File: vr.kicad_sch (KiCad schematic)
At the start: 23 parts, among them U2 ST1PS02CQTR, U3 ST1PS02CQTR, U301 LDLN025M12R, U304 LM2664M6_NOPB

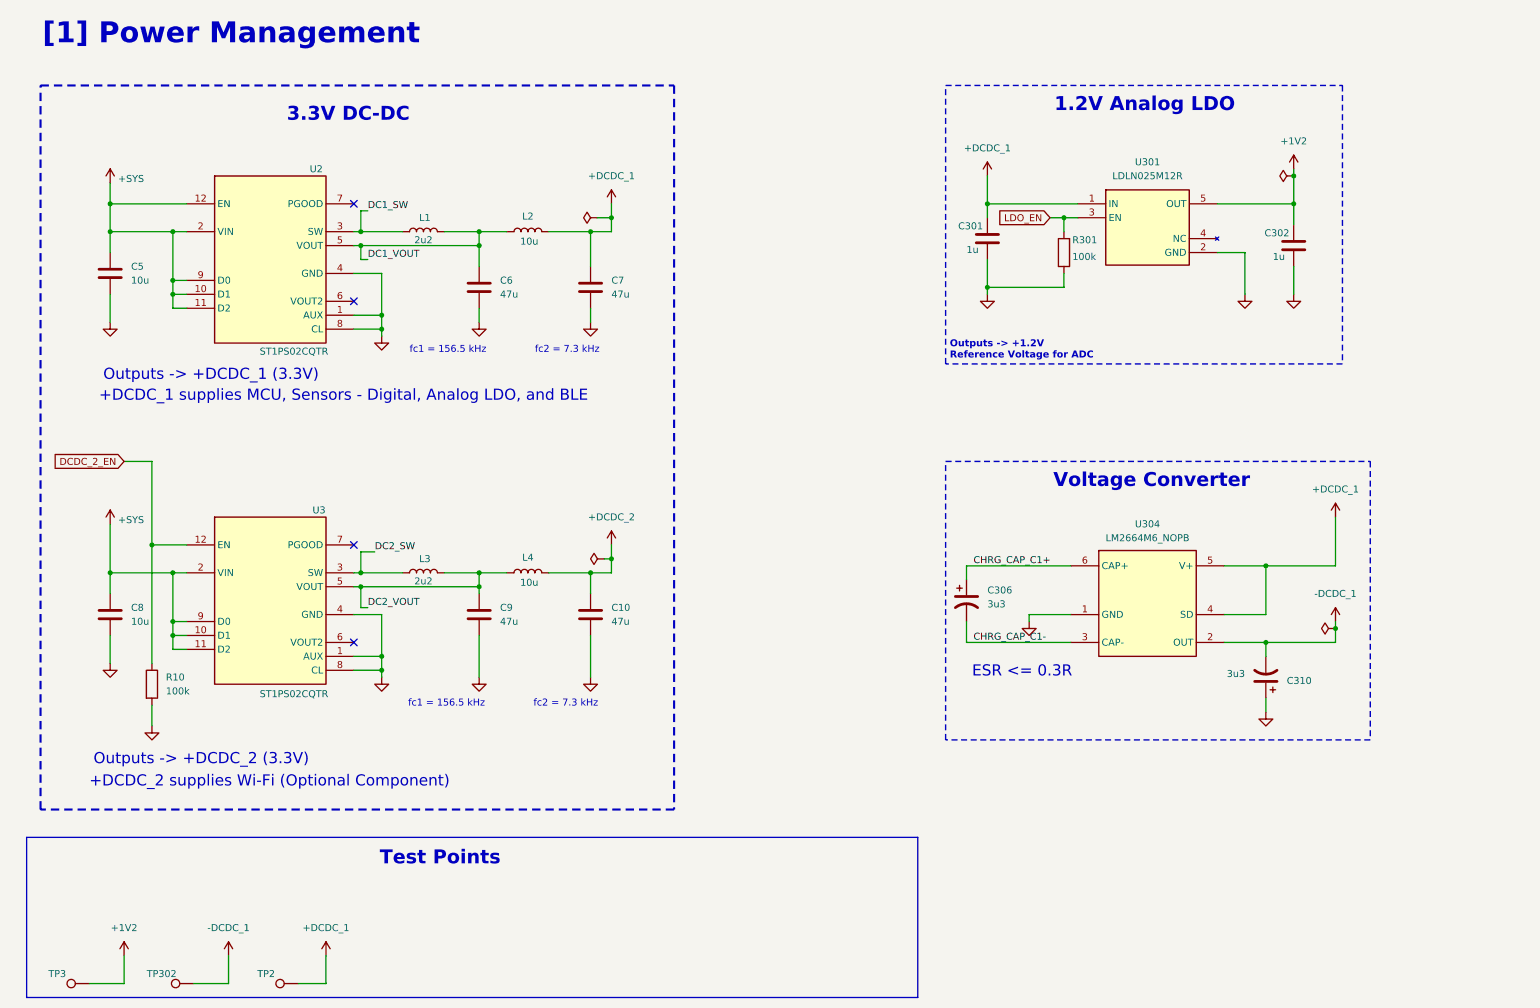
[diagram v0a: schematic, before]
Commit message: only usb powered
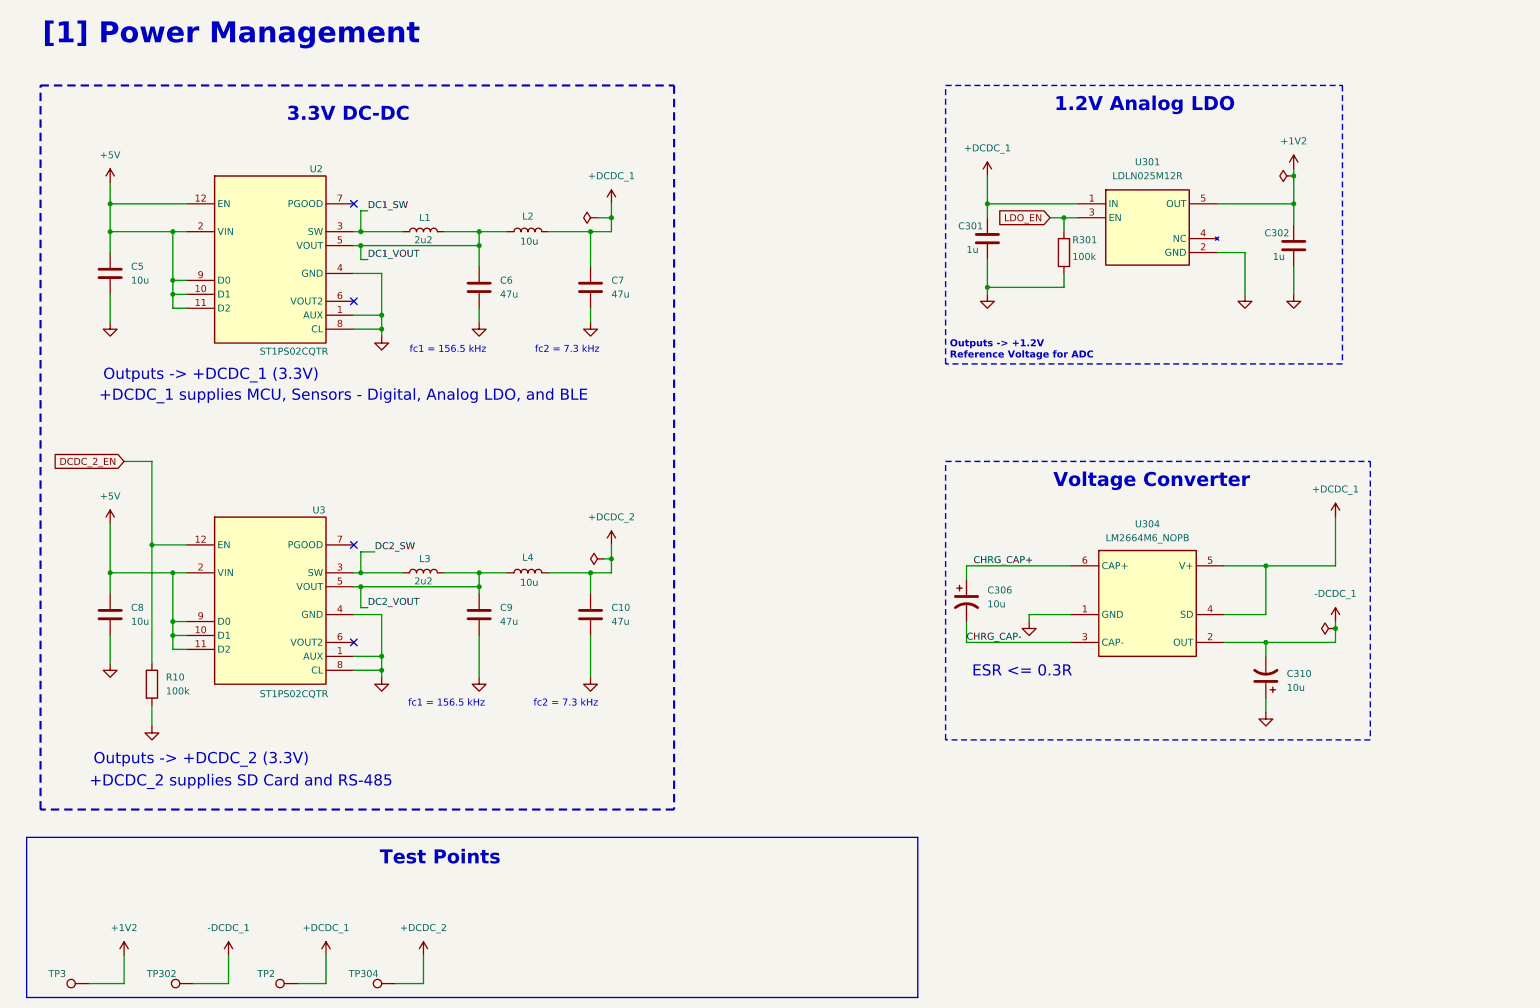
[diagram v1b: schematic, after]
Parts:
- added TP304: TestPoint, TestPoint:TestPoint_Loop_D3.50mm_Drill1.4mm_Beaded, symbol Connector:TestPoint
- C306, C310: value 3u3 -> 10u; footprint Capacitor_SMD:CP_Elec_4x3.9 -> EMS:10SVPS10M; Manufacturer_Name Nichicon -> Panasonic; Manufacturer_Part_Number UZG1H3R3MCL1GB -> 10SVPS10M
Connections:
- net +DCDC_2: now also TP304.1
- net +SYS renamed +5V
- net CHRG_CAP_C1+ renamed CHRG_CAP+
- net CHRG_CAP_C1- renamed CHRG_CAP-
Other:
- note added: "+DCDC_2 supplies SD Card and RS-485"
- note removed: "+DCDC_2 supplies Wi-Fi (Optional Component)"

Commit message: components with distributor links added
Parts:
- C10, C6, C7, C9: Distributor_Link (none) -> https://www.mouser.com/ProductDetail/KYOCERA-AVX/KGM15CR50J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; Manufacturer_Name (none) -> KYOCERA AVX; Manufacturer_Part_Number (none) -> KGM15CR50J476MT
- C301, C302: footprint Capacitor_SMD:C_0603_1608Metric -> Capacitor_SMD:C_0402_1005Metric; Distributor_Link (none) -> https://www.mouser.com/ProductDetail/KYOCERA-AVX/KGM05AR70J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; Manufacturer_Name (none) -> KYOCERA AVX; Manufacturer_Part_Number (none) -> KGM05AR70J105KH
- C306, C310: Distributor_Link (none) -> https://www.mouser.com/ProductDetail/Panasonic/10SVPS10M?qs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
- C5, C8: Distributor_Link (none) -> https://www.mouser.com/ProductDetail/KYOCERA-AVX/KGM15CR51A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; Manufacturer_Name (none) -> KYOCERA AVX; Manufacturer_Part_Number (none) -> KGM15CR51A106KT
- L1, L3: Distributor_Link (none) -> https://www.mouser.com/ProductDetail/TAIYO-YUDEN/MCHK1608T2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; Manufacturer_Name (none) -> TAIYO YUDEN; Manufacturer_Part_Number (none) -> MCHK1608T2R2MKN
- L2, L4: footprint Inductor_SMD:L_0603_1608Metric -> Inductor_SMD:L_0805_2012Metric; Distributor_Link (none) -> https://www.mouser.com/ProductDetail/Murata-Electronics/LQM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; Manufacturer_Name (none) -> Murata Electronics; Manufacturer_Part_Number (none) -> LQM21FN100M80L
- R10, R301: Distributor_Link (none) -> https://www.mouser.com/ProductDetail/Vishay-Dale/CRCW060310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; Manufacturer_Name (none) -> Vishay/Dale; Manufacturer_Part_Number (none) -> CRCW0603100KFKEE
- TP2, TP3, TP302, TP304: footprint TestPoint:TestPoint_Loop_D3.50mm_Drill1.4mm_Beaded -> EMS:5000; Distributor_Link (none) -> https://www.mouser.com/ProductDetail/Keystone-Electronics/5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; Manufacturer_Name (none) -> Keystone Electronics; Manufacturer_Part_Number (none) -> 5000
- U2, U3: Distributor_Link (none) -> https://www.mouser.co.uk/ProductDetail/STMicroelectronics/S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
- U301: Distributor_Link (none) -> https://www.mouser.co.uk/ProductDetail/STMicroelectronics/L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
- U304: Distributor_Link (none) -> https://www.mouser.co.uk/ProductDetail/Texas-Instruments/LM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

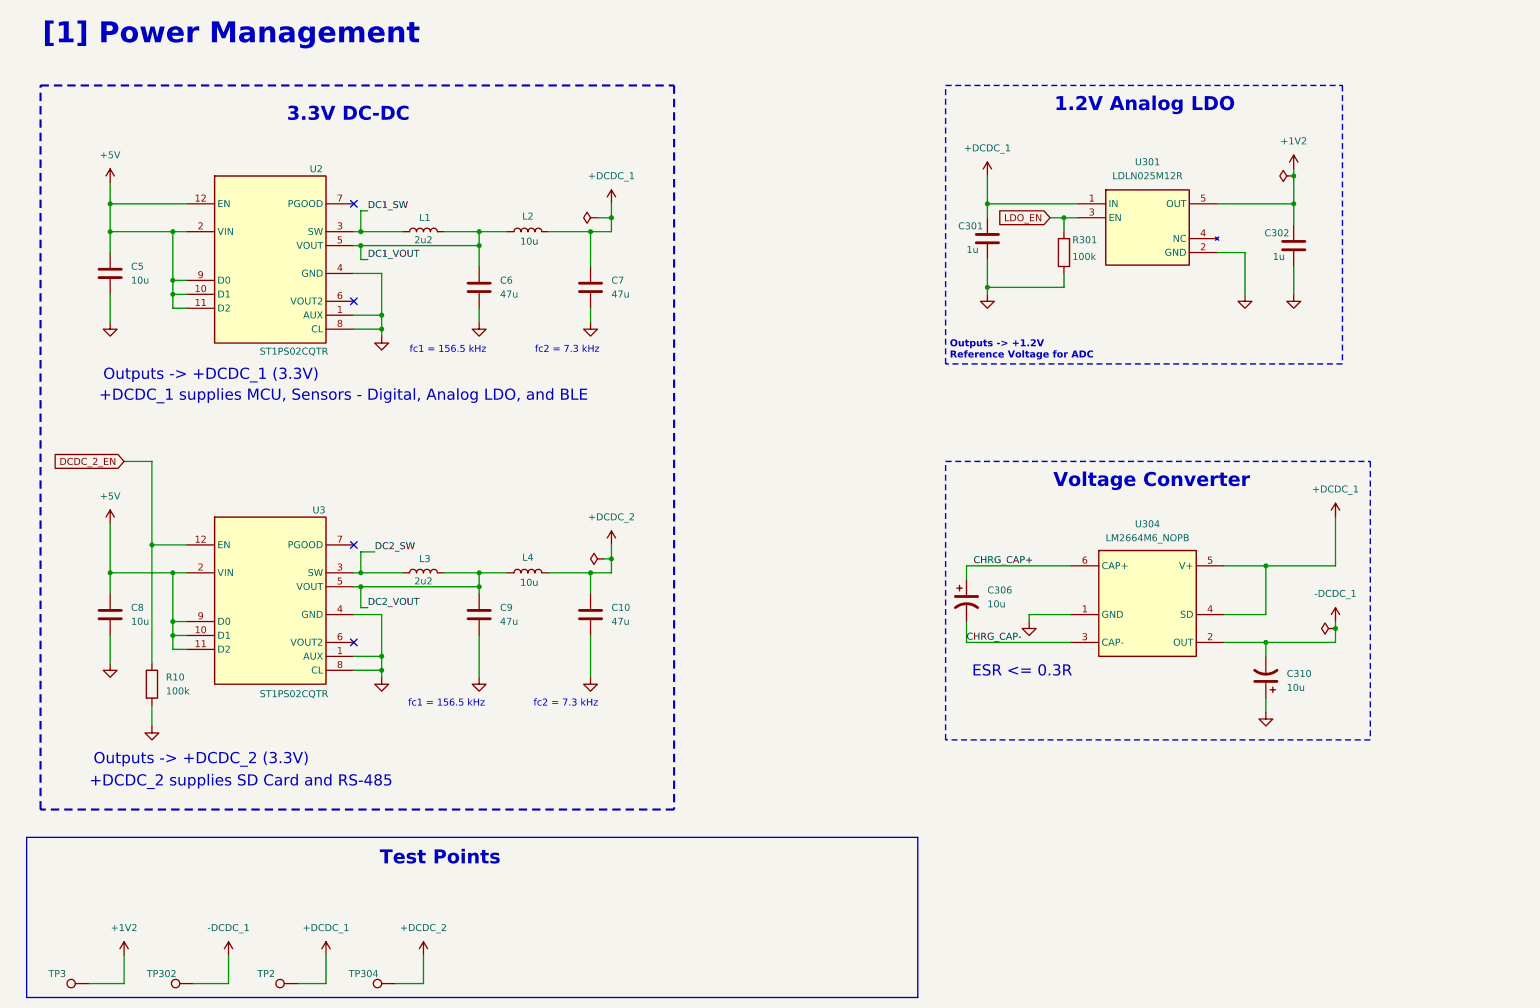
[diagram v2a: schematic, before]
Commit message: stitching vias and added power LEDs
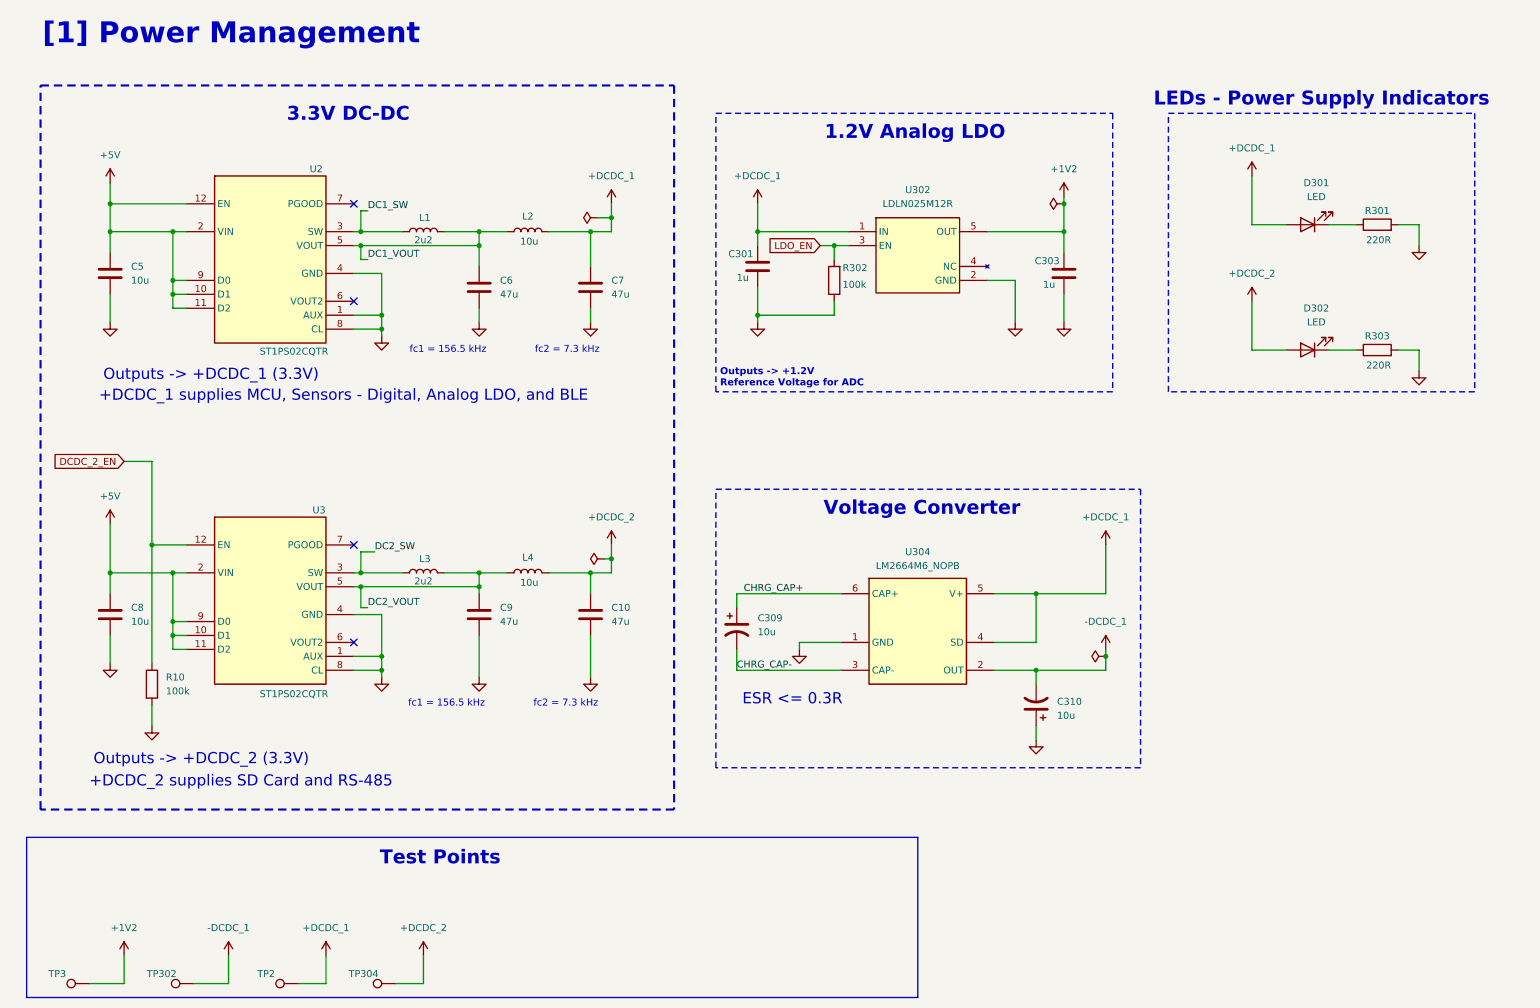
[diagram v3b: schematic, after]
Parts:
- added D301, D302: LED, LED_SMD:LED_0402_1005Metric, symbol Device:LED
- added R301, R303: 220R, Resistor_SMD:R_0402_1005Metric, symbol Device:R
- renumbered C302 to C303, C306 to C309, R301 to R302, U301 to U302
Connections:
- net +DCDC_1: now also D301.2 (A)
- net +DCDC_2: now also D302.2 (A)
- net GND: now also R301.2, R303.2
- new net: D301.1 (K), R301.1
- new net: D302.1 (K), R303.1
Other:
- note added: "LEDs - Power Supply Indicators"
- moved on the sheet: C301, C303, C309, C310, R302, U302, U304

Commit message: finalized design v1.0.0
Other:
- company: (none) -> Manufacturing Innovation Network Laboratory (MINLab)
- title: (none) -> Energy Monitoring System
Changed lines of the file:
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@@
 	(generator_version "8.0")
 	(paper "A4")
+	(title_block
+		(title "Energy Monitoring System")
+		(rev "v1.0.0")
+		(company "Manufacturing Innovation Network Laboratory (MINLab)")
+		(comment 1 "Developed by Vignesh Selvaraj")
+	)
 	(junction
 		(at 196.85 123.19)
@@
 		(dnp no)
 		(fields_autoplaced yes)
-		(property "Reference" "#PWR0312"
+		(property "Reference" "#PWR0313"
 			(at 201.93 80.01 0)
 			(effects
@@
 			(project "EnergyMonitoringSystem"
 				(path "/e660428c-c9b7-476c-8ac8-2d419f233469/609e23bd-fab9-4064-b1ef-0a1cfc73d358"
-					(reference "#PWR0312")
+					(reference "#PWR0313")
 					(unit 1)
 				)
@@
 		(dnp no)
 		(fields_autoplaced yes)
-		(property "Reference" "#PWR0302"
+		(property "Reference" "#PWR0303"
 			(at 208.28 56.388 0)
 			(effects
@@
 			(project "EnergyMonitoringSystem"
 				(path "/e660428c-c9b7-476c-8ac8-2d419f233469/609e23bd-fab9-4064-b1ef-0a1cfc73d358"
-					(reference "#PWR0302")
+					(reference "#PWR0303")
 					(unit 1)
 				)
@@
 			(project ""
 				(path "/e660428c-c9b7-476c-8ac8-2d419f233469/609e23bd-fab9-4064-b1ef-0a1cfc73d358"
-					(reference "#PWR0309")
+					(reference "#PWR0310")
 					(unit 1)
 				)
@@
 		(dnp no)
 		(fields_autoplaced yes)
-		(property "Reference" "#PWR0303"
+		(property "Reference" "#PWR0301"
 			(at 241.554 44.45 0)
 			(effects
@@
 			(project "EnergyMonitoringSystem"
 				(path "/e660428c-c9b7-476c-8ac8-2d419f233469/609e23bd-fab9-4064-b1ef-0a1cfc73d358"
-					(reference "#PWR0303")
+					(reference "#PWR0301")
 					(unit 1)
 				)
@@
 		(dnp no)
 		(fields_autoplaced yes)
-		(property "Reference" "#PWR0311"
+		(property "Reference" "#PWR0312"
 			(at 193.04 80.01 0)
 			(effects
@@
 			(project "EnergyMonitoringSystem"
 				(path "/e660428c-c9b7-476c-8ac8-2d419f233469/609e23bd-fab9-4064-b1ef-0a1cfc73d358"
-					(reference "#PWR0311")
+					(reference "#PWR0312")
 					(unit 1)
 				)
@@
 		(dnp no)
 		(fields_autoplaced yes)
-		(property "Reference" "#PWR0313"
+		(property "Reference" "#PWR0307"
 			(at 236.22 69.85 0)
 			(effects
@@
 			(project "EnergyMonitoringSystem"
 				(path "/e660428c-c9b7-476c-8ac8-2d419f233469/609e23bd-fab9-4064-b1ef-0a1cfc73d358"
-					(reference "#PWR0313")
+					(reference "#PWR0307")
 					(unit 1)
 				)
@@
 		(dnp no)
 		(fields_autoplaced yes)
-		(property "Reference" "#PWR0301"
+		(property "Reference" "#PWR0302"
 			(at 27.94 52.07 0)
 			(effects
@@
 			(project "EnergyMonitoringSystem"
 				(path "/e660428c-c9b7-476c-8ac8-2d419f233469/609e23bd-fab9-4064-b1ef-0a1cfc73d358"
-					(reference "#PWR0301")
+					(reference "#PWR0302")
 					(unit 1)
 				)
@@
 			(project ""
 				(path "/e660428c-c9b7-476c-8ac8-2d419f233469/609e23bd-fab9-4064-b1ef-0a1cfc73d358"
-					(reference "#PWR0308")
+					(reference "#PWR0309")
 					(unit 1)
 				)
@@
 		(dnp no)
 		(fields_autoplaced yes)
-		(property "Reference" "#PWR0310"
+		(property "Reference" "#PWR0311"
 			(at 146.05 80.01 0)
 			(effects
@@
 			(project "EnergyMonitoringSystem"
 				(path "/e660428c-c9b7-476c-8ac8-2d419f233469/609e23bd-fab9-4064-b1ef-0a1cfc73d358"
-					(reference "#PWR0310")
+					(reference "#PWR0311")
 					(unit 1)
 				)
@@
 			(project ""
 				(path "/e660428c-c9b7-476c-8ac8-2d419f233469/609e23bd-fab9-4064-b1ef-0a1cfc73d358"
-					(reference "#PWR0307")
+					(reference "#PWR0308")
 					(unit 1)
 				)

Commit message: minor formatting updates
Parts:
- TP2, TP3, TP302, TP304: footprint EMS:5000 -> TestPoint:TestPoint_Pad_D3.0mm
- renumbered C309 to C307, C301 to C308, C310 to C309, C303 to C310, R301 to R303, R303 to R304, U302 to U303
